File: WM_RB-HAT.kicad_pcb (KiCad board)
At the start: 4 copper layers, 65 x 30 mm, 61 parts, among them J1 AudioJack3, J2 AudioJack3, J3 2x20 Pins, J4 AudioJack3, J5 AudioJack3, J6 Audio In, J7 Audio Out, Q1 BC817, SW1 SSSS213202, U1 WM8960, U4 MCP1711T-33 /OT

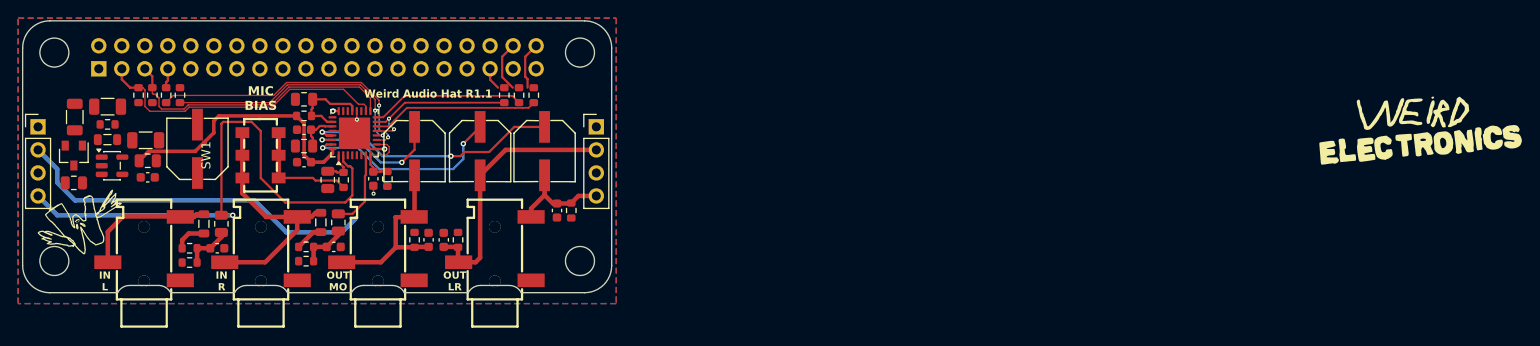
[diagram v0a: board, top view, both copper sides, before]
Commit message: Zone clearance 0.3→0.2mm, add silkscreen SVGs
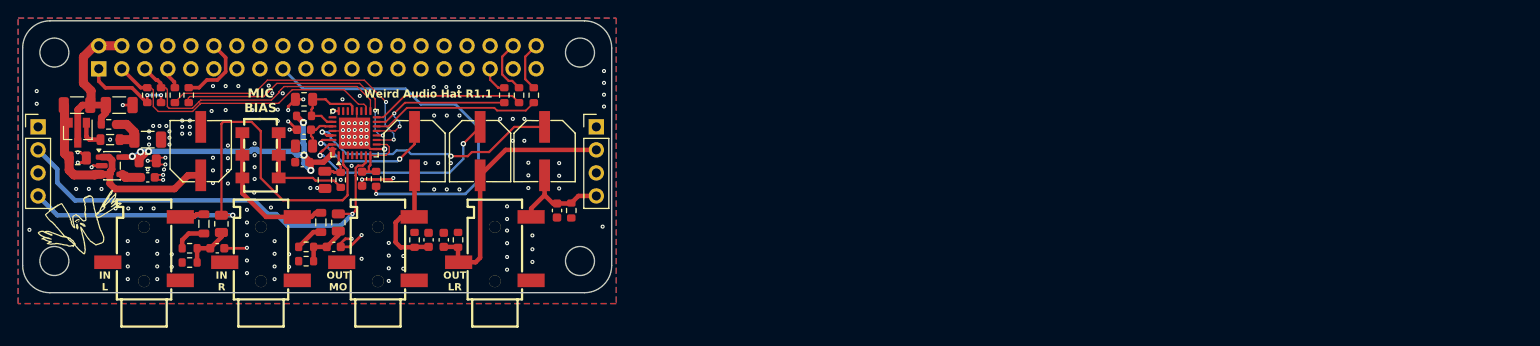
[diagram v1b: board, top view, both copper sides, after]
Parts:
- removed the G*** at (232.1, 71.7)
- C36: value 1uF X7R -> 4.7uF X7R
- moved C32 2.78 mm to (84.6, 75.4), turned to 0 degrees
- moved Q1 2.56 mm to (84.6, 72.6)
- moved R11 1.34 mm to (84.5, 69.6), turned to 0 degrees
- moved C35 1.29 mm to (89.2, 69.6)
- moved C3 1.25 mm to (116.0, 77.7)
- moved R27 1.25 mm to (117.5, 77.7)
- moved R13 0.96 mm to (93.8, 68.5)
- moved R14 0.96 mm to (92.2, 68.5)
- moved R2 0.96 mm to (96.8, 68.5)
- moved R26 0.96 mm to (95.3, 68.5)
- moved CP3 0.44 mm to (98.2, 74.7)
- moved C2 0.32 mm to (111.8, 77.9)
- moved R15 0.32 mm to (113.6, 77.9)
- moved FB3 0.29 mm to (88.2, 73.4)
- moved C22 0.24 mm to (92.3, 73.4)
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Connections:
- J1 pad R: /INPUT_R -> unconnected-(J1-PadR)
- J2 pad R: /OUT_MONO_AC -> unconnected-(J2-PadR)
- J5 pad R: /INPUT_L -> unconnected-(J5-PadR)
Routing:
- net +3.3V: track 0.00 -> 42.9 mm, vias 0 -> 1
- net +VREGIN: track 0.00 -> 27.0 mm
- net GND: track 10.6 -> 36.2 mm, vias 4 -> 163
- net +5V: track 0.00 -> 19.7 mm
- net /INPUT_L: track 14.8 -> 2.80 mm
- net /INPUT_R: track 27.5 -> 16.6 mm
- net /P3V3_HAT: track 0.00 -> 10.8 mm, vias 0 -> 2
- net /I2S_CLK: track 0.00 -> 8.26 mm
- net /OUT_MONO_AC: track 20.3 -> 13.0 mm
- net +3.3VA: track 29.3 -> 36.0 mm, vias 0 -> 6
- net Net-(C22-Pad1): track 0.00 -> 4.79 mm
- net Net-(Q1-B): track 0.00 -> 3.23 mm
- net Net-(U4-SENSE/ADJ): track 0.00 -> 2.17 mm
- net /HP_R: track 22.5 -> 24.2 mm
- net /I2C_SDA: track 32.9 -> 31.8 mm
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- removed copper zone on In2.Cu, net +5V
- removed copper zone on In2.Cu, net +VREGIN
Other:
- outline, holes or cut-outs redrawn
- board text removed: "${REFERENCE}"

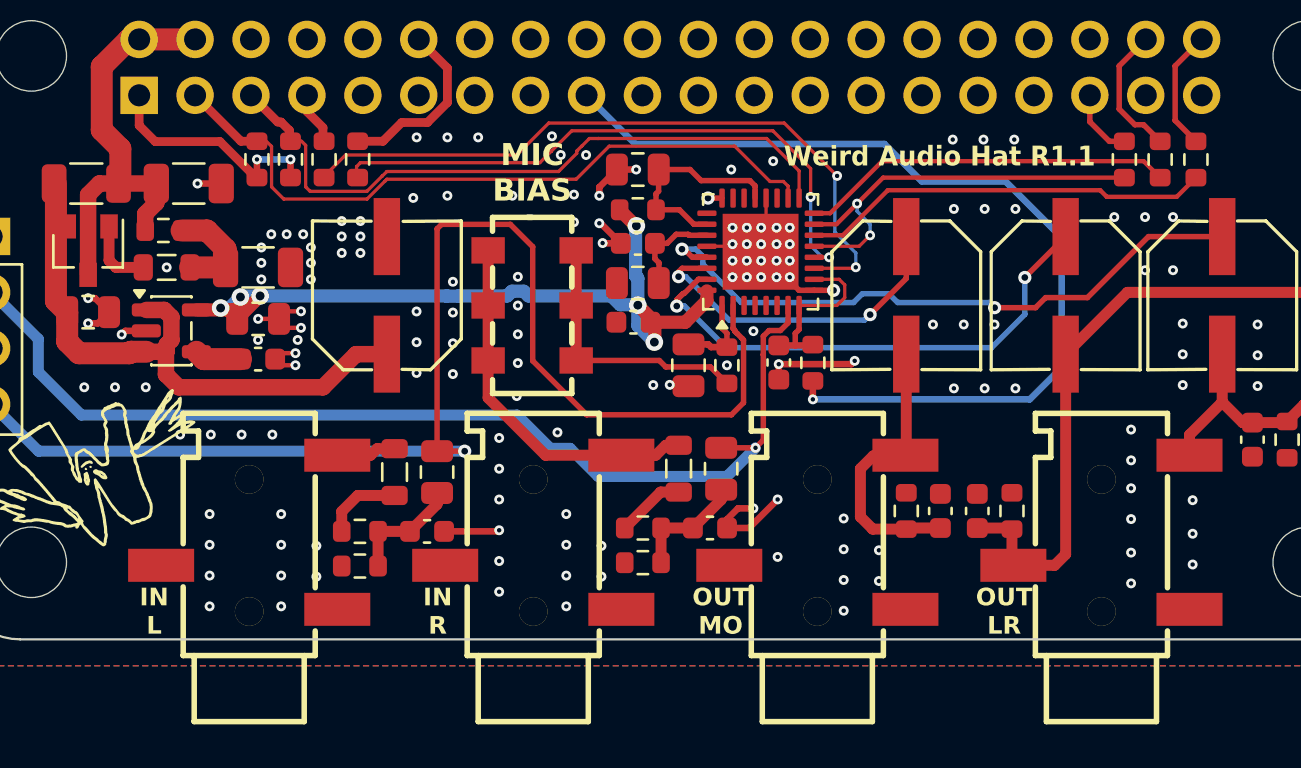
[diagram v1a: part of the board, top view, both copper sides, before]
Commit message: R1.1: HP output filter 100k→0Ω, silk labels OUT L/R, MIC-R BIAS
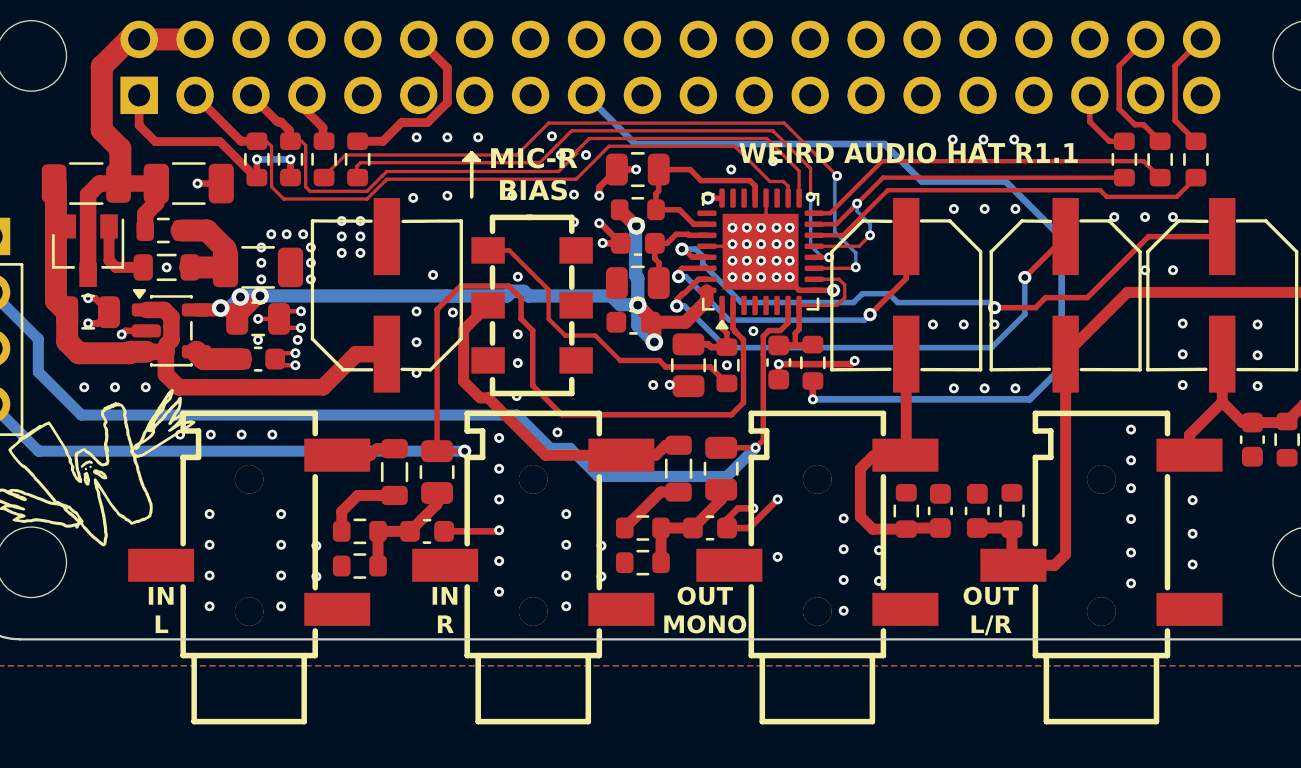
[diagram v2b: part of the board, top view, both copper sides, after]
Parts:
- R22, R23, R6: value 100K -> 0R
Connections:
- SW1 pad 1: /INPUT_R -> unconnected-(SW1-Pad1)
- SW1 pad 3: /INPUT_R -> Net-(R15-Pad1)
- SW1 pad 4: Net-(R15-Pad1) -> unconnected-(SW1-Pad4)
- SW1 pad 5: Net-(R15-Pad1) -> unconnected-(SW1-Pad5)
- SW1 pad 6: Net-(R15-Pad1) -> unconnected-(SW1-Pad6)
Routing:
- net /LINE_INPUT_L: track 59.2 -> 53.7 mm
- net Net-(R15-Pad1): track 12.3 -> 14.1 mm
- net /INPUT_R: track 16.6 -> 15.3 mm
- net GND: vias 163 -> 160
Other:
- board text added: "MIC-R BIAS"
- board text added: "OUT L/R"
- board text added: "OUT MONO"
- board text added: "WEIRD AUDIO HAT R1.1"
- board text removed: "MIC BIAS"
- board text removed: "OUT LR"
- board text removed: "OUT MO"
- board text removed: "Weird Audio Hat R1.1"
